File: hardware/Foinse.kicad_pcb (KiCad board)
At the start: 6 copper layers, 60 x 60 mm, 109 parts, among them J1 ESQ-110-X-X-D, J15 39-29-1048, J3 PJ-063AH, J4 5023860570, Q1 IPD90P04P4L04ATMA1, Q2 IPD90P04P4L04ATMA1, U1 STM32F072C8Tx, U17 LTC4412xS6, U19 TPS56A37RPAR, U2 MPM3650CGQW-P, U4 TJA1051T-3, U5 TPS563203, U6 ACS71240KEXBLT-010B3, U7 ACS71240KEXBLT-010B3

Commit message: minor changes
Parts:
- removed C49: 4.7uf, Capacitor_SMD:C_0402_1005Metric
- removed R10, R9: 0Ω, Resistor_SMD:R_0402_1005Metric
- removed R11: 499kΩ, Resistor_SMD:R_0402_1005Metric
- removed R13: 33.2kΩ, Resistor_SMD:R_0402_1005Metric
- removed VR1: LT3045EDD_PBF, footprints:SON50P300X300X80-11N
- added U8: TLV75533PDRV, Package_SON:WSON-6-1EP_2x2mm_P0.65mm_EP1x1.6mm, F.Cu at (144.3, 102.3)
- 3V3: renamed from 3v3; value S2761-46R -> 3V3
- 5VL: value S2761-46R -> 5vLogic
- C50: value 4.7uf -> 1uf
- C51: value 10uf -> 1uf
- F1: value S2761-46R -> FAULT1
- F2: value S2761-46R -> FAULT2
- GND: value S2761-46R -> GND
- moved G*** 52.9 mm to (165.1, 95.3)
- moved S1 47.8 mm to (173.7, 108.1)
- moved F1 42.1 mm to (173.7, 104.3)
- moved 5VS 33.8 mm to (167.2, 104.3)
- moved F2 29.4 mm to (170.4, 104.3), turned to 180 degrees
- moved 3V3 26.0 mm to (163.9, 108.1)
- moved S2 18.4 mm to (170.4, 108.1), turned to 180 degrees
- moved 5VL 14.3 mm to (167.2, 108.1)
- moved C27 14.0 mm to (146.9, 99.5), turned to 90 degrees
- moved C28 13.6 mm to (151.9, 100.0), turned to -90 degrees
- moved XTAL1 12.3 mm to (149.4, 99.0), turned to 0 degrees
- moved C24 12.0 mm to (165.8, 68.0), turned to -90 degrees
- moved G*** 11.8 mm to (162.4, 102.6)
- moved C6 11.8 mm to (153.5, 98.5), turned to 0 degrees
- moved C5 11.7 mm to (146.1, 97.2), turned to 180 degrees
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- renumbered C+ to CAN+1, C- to CAN-1
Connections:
- C10 pad 2: Net-(C10-Pad2) -> Net-(U2-FB)
- C33 pad 1: AGND -> GND
- R4 pad 1: AGND -> GND
- R4 pad 2: Net-(C10-Pad2) -> Net-(U2-FB)
- R8 pad 1: Net-(C10-Pad2) -> Net-(U2-FB)
- U2 pad 16: Net-(U2-EN) -> 5V_LOGIC
- U2 pad 18: AGND -> GND
- U7 pad 1: 5VSERVO -> 5VSERVO_S
- U7 pad 2: 5VSERVO -> 5VSERVO_S
- U7 pad 3: 5VSERVO_S -> 5VSERVO
- U7 pad 4: 5VSERVO_S -> 5VSERVO
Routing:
- net 3.3V: track 142.9 -> 38.3 mm, vias 12 -> 10
- net Sense1: track 37.8 -> 0.95 mm, vias 2 -> 1
- net NRST: track 33.2 -> 6.46 mm
- net Fault1: track 29.4 -> 4.15 mm
- net SWCLK: track 26.7 -> 4.96 mm
- net 5VLOGIC: track 106.3 -> 84.8 mm, vias 6 -> 7
- net GND: track 41.0 -> 57.3 mm, vias 187 -> 183
- net SWDIO: track 21.4 -> 5.10 mm
- net 5V_LOGIC: track 1.59 -> 11.9 mm, vias 1 -> 3
- net Net-(U2-EN): track 9.96 -> 0.00 mm, vias 2 -> 0
- net CAN_-: track 5.96 -> 14.6 mm, vias 0 -> 1
- net CAN_+: track 5.99 -> 14.1 mm
- net Fault2: track 23.2 -> 29.7 mm
- net AGND: track 5.06 -> 0.00 mm
- net Net-(C10-Pad2): track 3.76 -> 0.00 mm
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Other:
- outline, holes or cut-outs redrawn

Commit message: minor changes
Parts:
- moved G*** 47.5 mm to (179.2, 104.5)
- moved G*** 11.0 mm to (137.5, 95.2)
- renumbered CAN+1 to CAN+, CAN-1 to CAN-
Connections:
- C11 pad 2: 5V_LOGIC -> 5VLOGIC
- C29 pad 2: 5V_LOGIC -> 5VLOGIC
- C30 pad 2: 5V_LOGIC -> 5VLOGIC
- U2 pad 16: 5V_LOGIC -> 5VLOGIC
- U2 pad 22: 5V_LOGIC -> 5VLOGIC
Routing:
- net 3.3V: track 38.3 -> 149.1 mm, vias 10 -> 12
- net 5VLOGIC: track 84.8 -> 171.8 mm, vias 7 -> 12
- net Sense1: track 0.95 -> 59.1 mm, vias 1 -> 3
- net Fault1: track 4.15 -> 59.6 mm, vias 2 -> 4
- net 5VSERVO_S: track 22.1 -> 57.8 mm, vias 2 -> 4
- net Fault2: track 29.7 -> 58.6 mm, vias 2 -> 3
- net Sense2: track 33.5 -> 55.5 mm, vias 2 -> 3
- net GND: track 57.3 -> 39.3 mm, vias 183 -> 189
- net SWCLK: track 4.96 -> 18.2 mm
- net SWDIO: track 5.10 -> 18.3 mm
- net 5V_LOGIC: track 11.9 -> 0.00 mm, vias 3 -> 0
- net NRST: track 6.46 -> 15.8 mm
- net Net-(U8-EN): track 7.72 -> 6.50 mm
- net CAN_-: vias 1 -> 0
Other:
- board text added: "I wish upon you ample doses of pain and suffering"

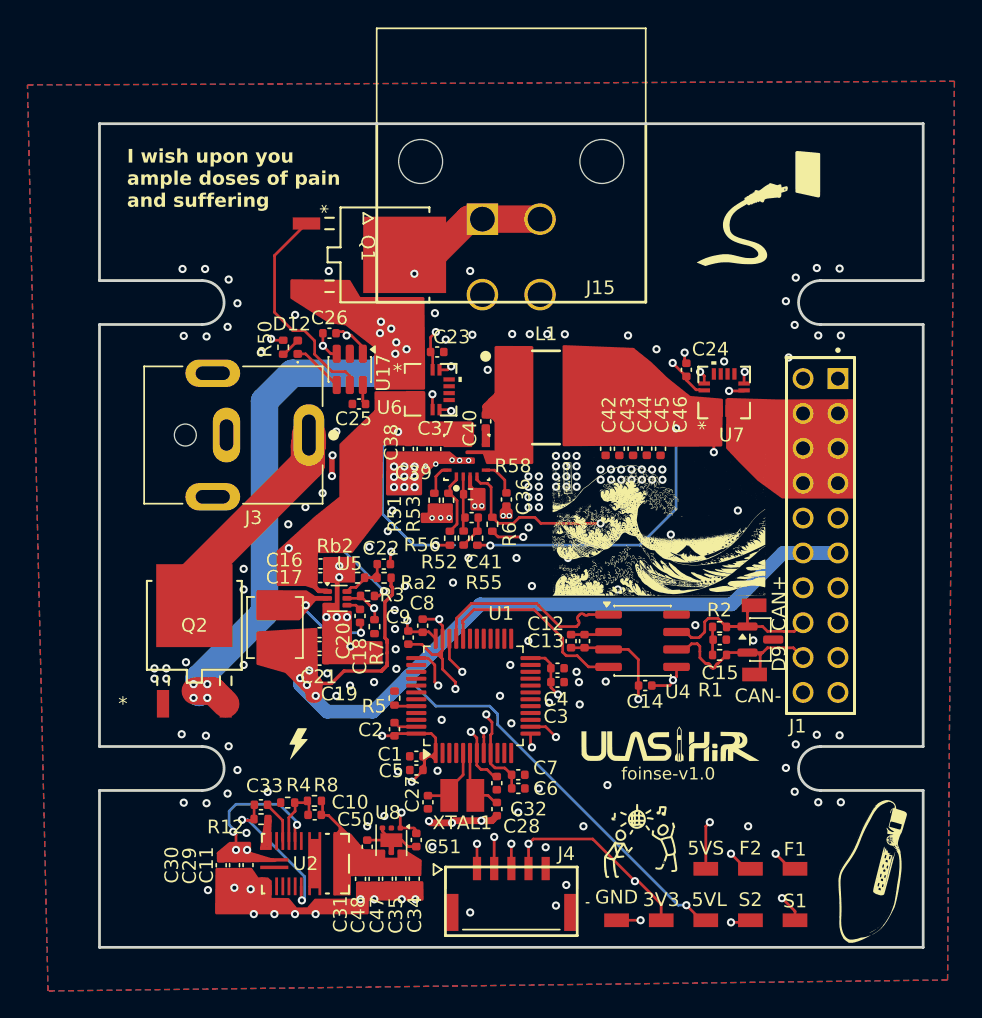
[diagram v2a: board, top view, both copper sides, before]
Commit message: added voltage sensing
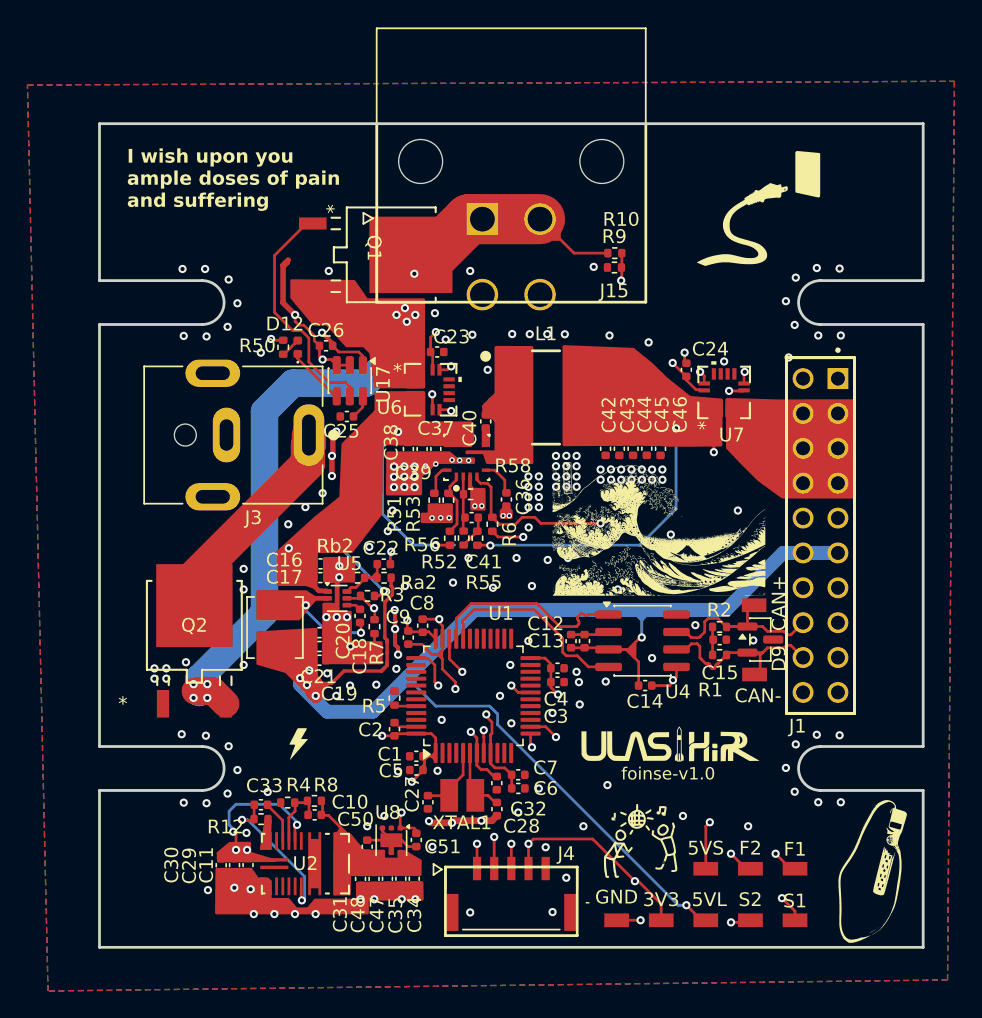
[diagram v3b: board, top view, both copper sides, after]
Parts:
- added R10: 240kΩ, Resistor_SMD:R_0402_1005Metric, F.Cu at (160.5, 59.5)
- added R9: 150kΩ, Resistor_SMD:R_0402_1005Metric, F.Cu at (160.5, 60.5)
- moved C25 1.26 mm to (141.0, 71.4)
- moved C26 0.95 mm to (139.5, 66.2)
- moved U17 0.83 mm to (141.2, 68.8)
- moved Q1 0.46 mm to (144.2, 59.6)
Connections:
- net Net-(Q1-D) renamed BAT
- U1 pad 19: unconnected-(U1-PB1-Pad19) -> Net-(U1-PB1)
- U1 pad 27: BATTERY_CURRENT_CS -> unconnected-(U1-PB14-Pad27)
- U1 pad 28: SERVO_CURRENT_CS -> unconnected-(U1-PB15-Pad28)
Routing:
- net Net-(U1-PB1): track 0.00 -> 36.6 mm, vias 0 -> 3
- net GND: track 39.3 -> 63.7 mm, vias 189 -> 193
- net BAT: track 20.6 -> 29.6 mm
- net pwr_s: track 38.8 -> 43.3 mm, vias 10 -> 8
- net Net-(Q1-G): track 16.1 -> 16.9 mm
- net Net-(D12-K): track 3.78 -> 4.33 mm

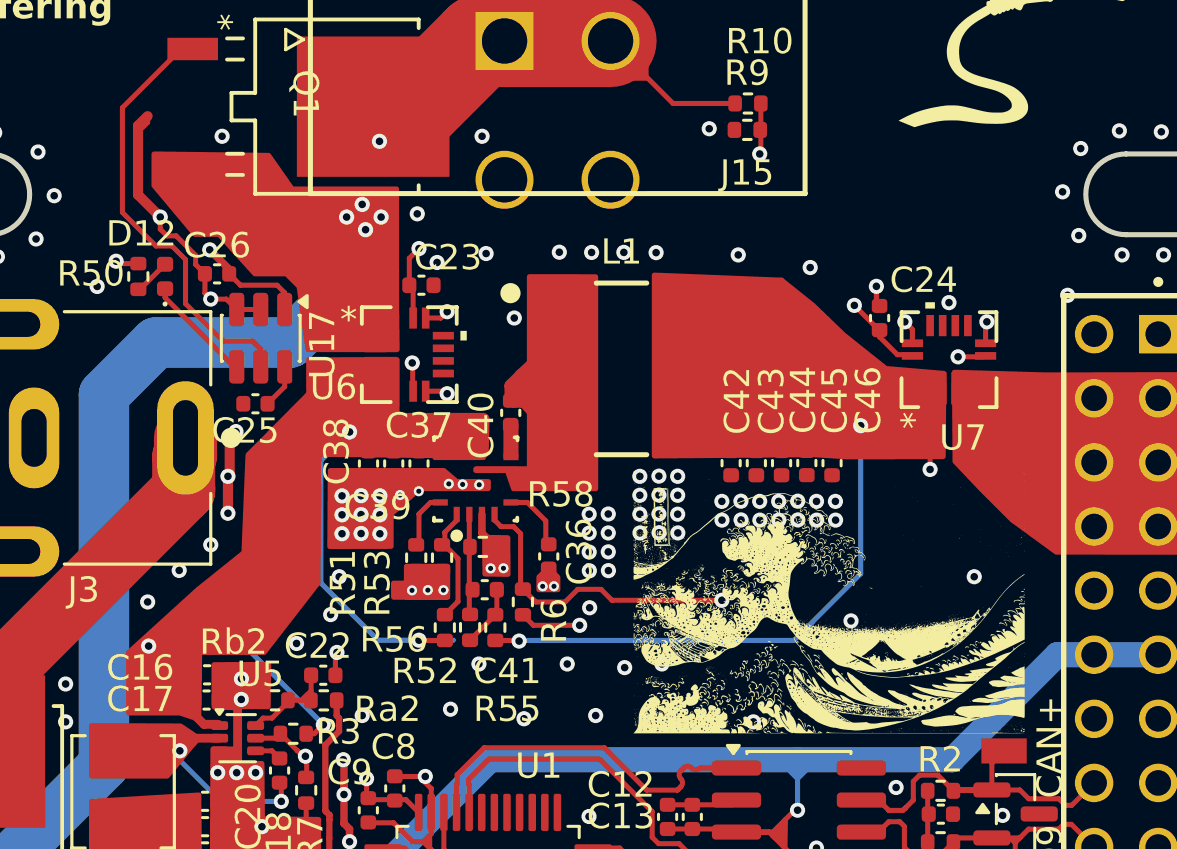
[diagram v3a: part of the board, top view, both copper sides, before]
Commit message: added voltage sensing
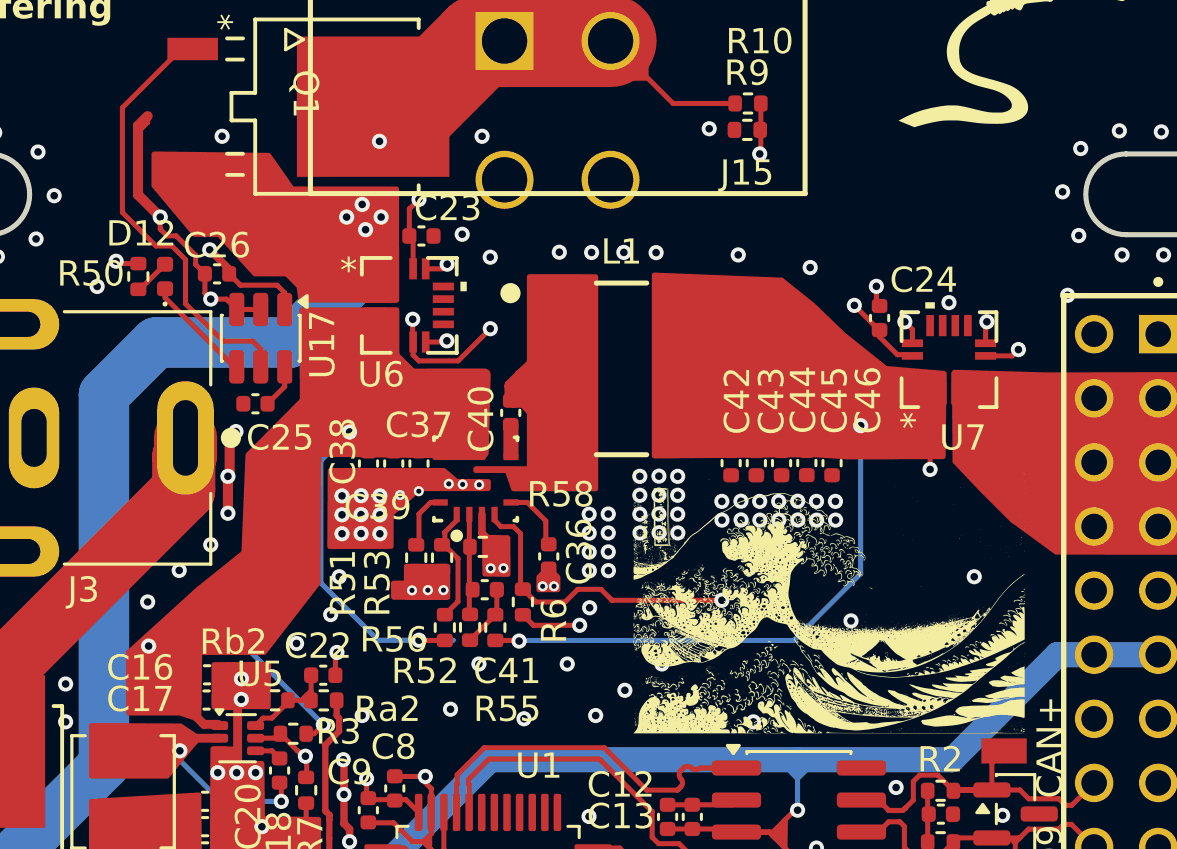
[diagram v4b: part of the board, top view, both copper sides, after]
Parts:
- moved C23 1.95 mm to (147.6, 64.8)
- moved U6 1.95 mm to (147.1, 67.5)
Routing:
- net GND: track 63.7 -> 68.0 mm, vias 193 -> 192
- net Fault1: track 59.9 -> 62.1 mm
- net Sense1: track 59.1 -> 61.0 mm
- net 3.3V: track 149.1 -> 150.9 mm
- net pwr: track 24.9 -> 25.8 mm
